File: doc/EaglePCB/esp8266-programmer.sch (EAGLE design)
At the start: 6 parts

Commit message: small fixes
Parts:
- R1, R2: value 10k -> 1k
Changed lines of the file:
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@@
 <part name="RST" library="SparkFun-Retired" deviceset="TAC_SWITCH" device="PTH"/>
 <part name="PRG" library="SparkFun-Retired" deviceset="TAC_SWITCH" device="PTH"/>
-<part name="R1" library="eagle-ltspice" deviceset="R" device="0207/10" value="10k"/>
-<part name="R2" library="eagle-ltspice" deviceset="R" device="0207/10" value="10k"/>
+<part name="R1" library="eagle-ltspice" deviceset="R" device="0207/10" value="1k"/>
+<part name="R2" library="eagle-ltspice" deviceset="R" device="0207/10" value="1k"/>
 </parts>
 <sheets>

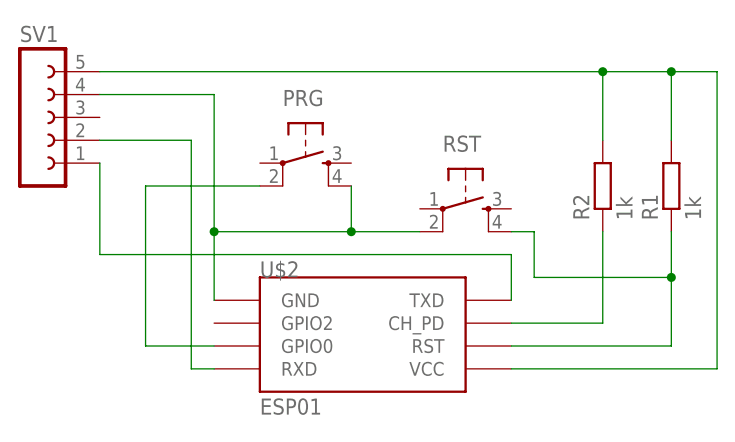
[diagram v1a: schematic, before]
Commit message: correct PCB design and add PIR IoT device
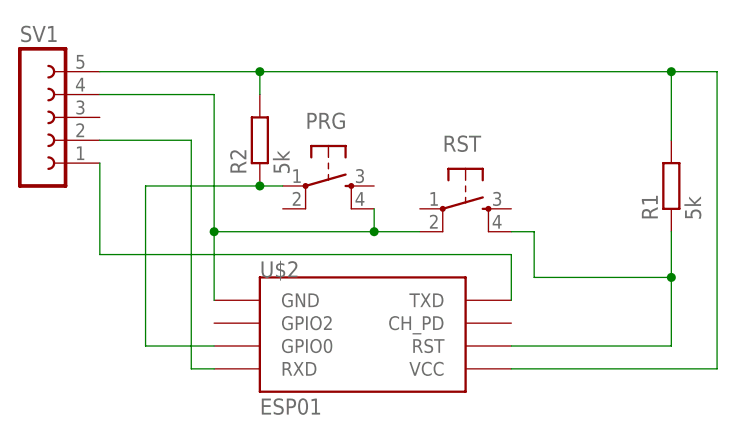
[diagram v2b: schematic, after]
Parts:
- R1, R2: value 1k -> 5k
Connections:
- removed net CH_PD: R2.1, U$2.CH_PD
- net GPIO0: now also PRG.1, R2.1; no longer PRG.2
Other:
- moved on the sheet: PRG, R2
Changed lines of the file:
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@@
 <part name="RST" library="SparkFun-Retired" deviceset="TAC_SWITCH" device="PTH"/>
 <part name="PRG" library="SparkFun-Retired" deviceset="TAC_SWITCH" device="PTH"/>
-<part name="R1" library="eagle-ltspice" deviceset="R" device="0207/10" value="1k"/>
-<part name="R2" library="eagle-ltspice" deviceset="R" device="0207/10" value="1k"/>
+<part name="R1" library="eagle-ltspice" deviceset="R" device="0207/10" value="5k"/>
+<part name="R2" library="eagle-ltspice" deviceset="R" device="0207/10" value="5k"/>
 </parts>
 <sheets>
@@
 <instance part="U$2" gate="G$1" x="35.56" y="43.18"/>
 <instance part="RST" gate="S" x="45.72" y="60.96"/>
-<instance part="PRG" gate="S" x="27.94" y="66.04"/>
+<instance part="PRG" gate="S" x="30.48" y="63.5"/>
 <instance part="R1" gate="G$1" x="68.58" y="63.5" rot="R90"/>
-<instance part="R2" gate="G$1" x="60.96" y="63.5" rot="R90"/>
+<instance part="R2" gate="G$1" x="22.86" y="68.58" rot="R90"/>
 </instances>
 <busses>
@@
 <wire x1="17.78" y1="58.42" x2="17.78" y2="50.8" width="0.1524" layer="91"/>
 <pinref part="RST" gate="S" pin="2"/>
-<wire x1="17.78" y1="58.42" x2="33.02" y2="58.42" width="0.1524" layer="91"/>
-<junction x="33.02" y="58.42"/>
-<wire x1="33.02" y1="58.42" x2="40.64" y2="58.42" width="0.1524" layer="91"/>
+<wire x1="17.78" y1="58.42" x2="35.56" y2="58.42" width="0.1524" layer="91"/>
+<junction x="35.56" y="58.42"/>
+<wire x1="35.56" y1="58.42" x2="40.64" y2="58.42" width="0.1524" layer="91"/>
 <pinref part="PRG" gate="S" pin="4"/>
-<wire x1="33.02" y1="63.5" x2="33.02" y2="58.42" width="0.1524" layer="91"/>
+<wire x1="35.56" y1="60.96" x2="35.56" y2="58.42" width="0.1524" layer="91"/>
 </segment>
 </net>
@@
 <segment>
 <pinref part="SV1" gate="G$1" pin="5"/>
-<wire x1="5.08" y1="76.2" x2="60.96" y2="76.2" width="0.1524" layer="91"/>
-<wire x1="60.96" y1="76.2" x2="68.58" y2="76.2" width="0.1524" layer="91"/>
+<wire x1="5.08" y1="76.2" x2="22.86" y2="76.2" width="0.1524" layer="91"/>
+<wire x1="22.86" y1="76.2" x2="68.58" y2="76.2" width="0.1524" layer="91"/>
 <wire x1="68.58" y1="76.2" x2="73.66" y2="76.2" width="0.1524" layer="91"/>
 <wire x1="73.66" y1="76.2" x2="73.66" y2="43.18" width="0.1524" layer="91"/>
@@
 <wire x1="73.66" y1="43.18" x2="50.8" y2="43.18" width="0.1524" layer="91"/>
 <pinref part="R2" gate="G$1" pin="2"/>
-<wire x1="60.96" y1="68.58" x2="60.96" y2="76.2" width="0.1524" layer="91"/>
-<junction x="60.96" y="76.2"/>
+<wire x1="22.86" y1="73.66" x2="22.86" y2="76.2" width="0.1524" layer="91"/>
+<junction x="22.86" y="76.2"/>
 <junction x="68.58" y="76.2"/>
 <pinref part="R1" gate="G$1" pin="2"/>
@@
 <wire x1="5.08" y1="55.88" x2="50.8" y2="55.88" width="0.1524" layer="91"/>
 <wire x1="50.8" y1="55.88" x2="50.8" y2="50.8" width="0.1524" layer="91"/>
-</segment>
-</net>
-<net name="CH_PD" class="0">
-<segment>
-<pinref part="U$2" gate="G$1" pin="CH_PD"/>
-<pinref part="R2" gate="G$1" pin="1"/>
-<wire x1="50.8" y1="48.26" x2="60.96" y2="48.26" width="0.1524" layer="91"/>
-<wire x1="60.96" y1="48.26" x2="60.96" y2="58.42" width="0.1524" layer="91"/>
 </segment>
 </net>
@@
 <wire x1="17.78" y1="45.72" x2="10.16" y2="45.72" width="0.1524" layer="91"/>
 <wire x1="10.16" y1="45.72" x2="10.16" y2="63.5" width="0.1524" layer="91"/>
+<pinref part="R2" gate="G$1" pin="1"/>
 <wire x1="10.16" y1="63.5" x2="22.86" y2="63.5" width="0.1524" layer="91"/>
-<pinref part="PRG" gate="S" pin="2"/>
+<pinref part="PRG" gate="S" pin="1"/>
+<wire x1="22.86" y1="63.5" x2="25.4" y2="63.5" width="0.1524" layer="91"/>
+<junction x="22.86" y="63.5"/>
 </segment>
 </net>
